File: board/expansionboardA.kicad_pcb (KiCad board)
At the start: 2 copper layers, 131 x 83.8 mm, 55 parts, among them J1 USB_C_Receptacle, J3 HDMI_A, SW4 ESPPROG, U1 ESP32-S3-WROOM-1, U2 GPIO_U2, U3 SII164CTG64, U4 GPIO_U4, U6 CS4344-CZZR

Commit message: Updates to board files
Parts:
- added REF**: Fiducial_0.5mm_Mask1.5mm, Fiducial:Fiducial_0.5mm_Mask1.5mm, B.Cu at (130.9, 78.7)
- added REF**: Fiducial_0.5mm_Mask1.5mm, Fiducial:Fiducial_0.5mm_Mask1.5mm, B.Cu at (74.5, 61.3)
- added REF**: Fiducial_0.5mm_Mask1.5mm, Fiducial:Fiducial_0.5mm_Mask1.5mm, B.Cu at (122.2, 59.7)
- added REF**: Fiducial_0.5mm_Mask1.5mm, Fiducial:Fiducial_0.5mm_Mask1.5mm, B.Cu at (132.6, 96.2)
- added REF**: Fiducial_0.5mm_Mask1.5mm, Fiducial:Fiducial_0.5mm_Mask1.5mm, B.Cu at (98.2, 74.2)
- added REF**: Fiducial_0.5mm_Mask1.5mm, Fiducial:Fiducial_0.5mm_Mask1.5mm, B.Cu at (32.0, 65.9)
- added t3V3: TestPoint, TestPoint:TestPoint_Pad_D1.0mm, B.Cu at (135.6, 53.2)
- added t5V0: TestPoint, TestPoint:TestPoint_Pad_D1.0mm, B.Cu at (112.6, 43.2)
- added tEN1: TestPoint, TestPoint:TestPoint_Pad_D1.0mm, B.Cu at (80.0, 52.5)
- added tPWR1: TestPoint, TestPoint:TestPoint_Pad_D1.0mm, B.Cu at (31.8, 91.1)
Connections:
- REF** pad 1: SHLD -> GND (x4)
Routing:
- net 5V: track 173.1 -> 180.1 mm
- net ESP_RST: track 42.2 -> 45.8 mm
- net REG3V3: track 228.3 -> 231.0 mm

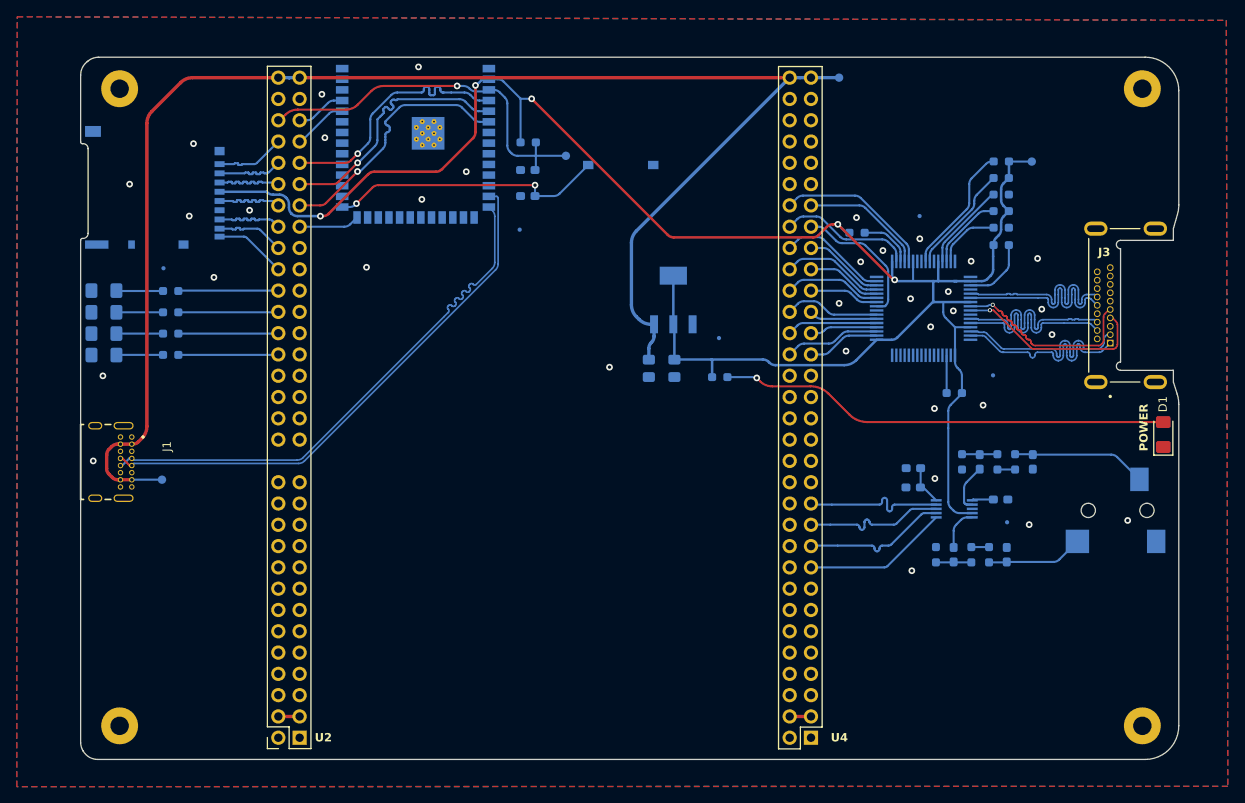
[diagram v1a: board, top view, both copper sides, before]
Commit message: Updated board and some typos in doc
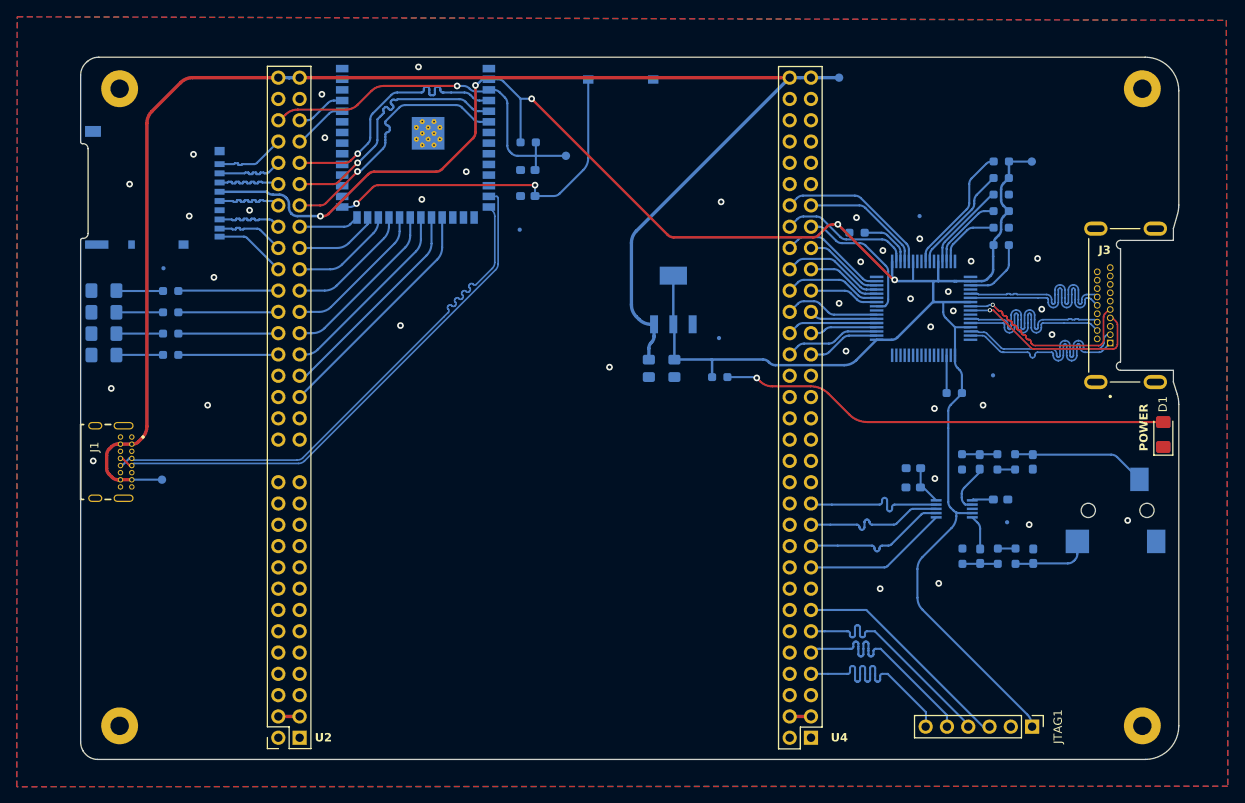
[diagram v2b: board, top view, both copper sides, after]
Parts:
- added JTAG1: Conn_01x06_Pin, Connector_PinHeader_2.54mm:PinHeader_1x06_P2.54mm_Vertical, F.Cu at (135.6, 120.6)
- moved REF** 52.1 mm to (78.0, 118.1)
- moved REF** 52.1 mm to (89.8, 118.4)
- moved REF** 52.1 mm to (83.9, 118.0)
- moved REF** 52.1 mm to (67.4, 118.0)
- moved SW4 10.2 mm to (86.5, 43.4)
- moved C13 3.17 mm to (129.4, 100.3)
- moved C9 3.17 mm to (135.7, 100.3)
- moved R12 3.17 mm to (131.5, 100.3)
- moved R8 3.17 mm to (133.6, 100.3)
- moved R11 3.17 mm to (127.3, 100.3)
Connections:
- U1 pad 18: unconnected-(U1-IO10-Pad18) -> IO10
- U1 pad 19: unconnected-(U1-IO11-Pad19) -> IO11
- U1 pad 20: unconnected-(U1-IO12-Pad20) -> IO12
- U1 pad 21: unconnected-(U1-IO13-Pad21) -> IO13
- U1 pad 22: unconnected-(U1-IO14-Pad22) -> IO14
- U1 pad 23: unconnected-(U1-IO21-Pad23) -> IO21
- U1 pad 24: unconnected-(U1-IO47-Pad24) -> IO47
- U1 pad 25: unconnected-(U1-IO48-Pad25) -> IO48
- U2 pad 33: unconnected-(U2-Pin_33-Pad33) -> IO10
- U2 pad 35: unconnected-(U2-Pin_35-Pad35) -> IO11
- U2 pad 37: unconnected-(U2-Pin_37-Pad37) -> IO12
- U2 pad 39: unconnected-(U2-Pin_39-Pad39) -> IO13
- U2 pad 41: unconnected-(U2-Pin_41-Pad41) -> IO14
- U2 pad 43: unconnected-(U2-Pin_43-Pad43) -> IO21
- U2 pad 45: unconnected-(U2-Pin_45-Pad45) -> IO47
- U2 pad 47: unconnected-(U2-Pin_47-Pad47) -> IO48
- U4 pad 11: unconnected-(U4-Pin_11-Pad11) -> TDO
- U4 pad 13: unconnected-(U4-Pin_13-Pad13) -> TCK
- U4 pad 7: unconnected-(U4-Pin_7-Pad7) -> TMS
- U4 pad 9: unconnected-(U4-Pin_9-Pad9) -> TDI
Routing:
- net REG3V3: track 231.0 -> 263.8 mm
- net IO10: track 0.00 -> 28.4 mm
- net TCK: track 0.00 -> 27.1 mm
- net TDO: track 0.00 -> 27.0 mm
- net TDI: track 0.00 -> 27.0 mm
- net TMS: track 0.00 -> 26.9 mm
- net IO11: track 0.00 -> 25.8 mm
- net IO12: track 0.00 -> 23.1 mm
- net IO13: track 0.00 -> 20.5 mm
- net IO14: track 0.00 -> 17.9 mm
- net IO21: track 0.00 -> 15.2 mm
- net IO47: track 0.00 -> 13.0 mm
- net Net-(U1-IO0): track 33.1 -> 43.2 mm
- net IO48: track 0.00 -> 10.00 mm
- net Net-(AU1-Pad2): track 11.5 -> 9.50 mm
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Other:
- board text added: "DVI 1.0"
- board text removed: "AA1"
- board text removed: "AA19"
- board text removed: "AA20"
- board text removed: "AA3"
- board text removed: "AB1"
- board text removed: "AB2"
- board text removed: "AB21"
- board text removed: "AB3"
- board text removed: "DVI 1.0 OUT"
- board text removed: "ESP32-S3-WROOM-1"
- board text removed: "H2"
- board text removed: "K1"
- board text removed: "K2"
- board text removed: "M1"
- board text removed: "N17"
- board text removed: "POWER & DATA"
- board text removed: "R18"
- board text removed: "R4"
- board text removed: "T1"
- board text removed: "T21"
- board text removed: "T4"
- board text removed: "T5"
- board text removed: "U1"
- board text removed: "U17"
- board text removed: "U20"
- board text removed: "U5"
- board text removed: "V18"
- board text removed: "V4"
- board text removed: "W1"
- board text removed: "W4"
- board text removed: "Y1"
- board text removed: "Y18"
- board text removed: "Y21"
- board text removed: "Y3"

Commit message: Board update
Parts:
- added REF**: Fiducial_0.5mm_Mask1.5mm, Fiducial:Fiducial_0.5mm_Mask1.5mm, B.Cu at (143.6, 44.2)
- added REF**: Fiducial_0.5mm_Mask1.5mm, Fiducial:Fiducial_0.5mm_Mask1.5mm, B.Cu at (143.4, 120.1)
- added REF**: Fiducial_0.5mm_Mask1.5mm, Fiducial:Fiducial_0.5mm_Mask1.5mm, B.Cu at (31.8, 44.2)
- added REF**: Fiducial_0.5mm_Mask1.5mm, Fiducial:Fiducial_0.5mm_Mask1.5mm, B.Cu at (31.8, 120.1)
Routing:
- net REG3V3: track 263.8 -> 264.7 mm
- net GND: vias 37 -> 42

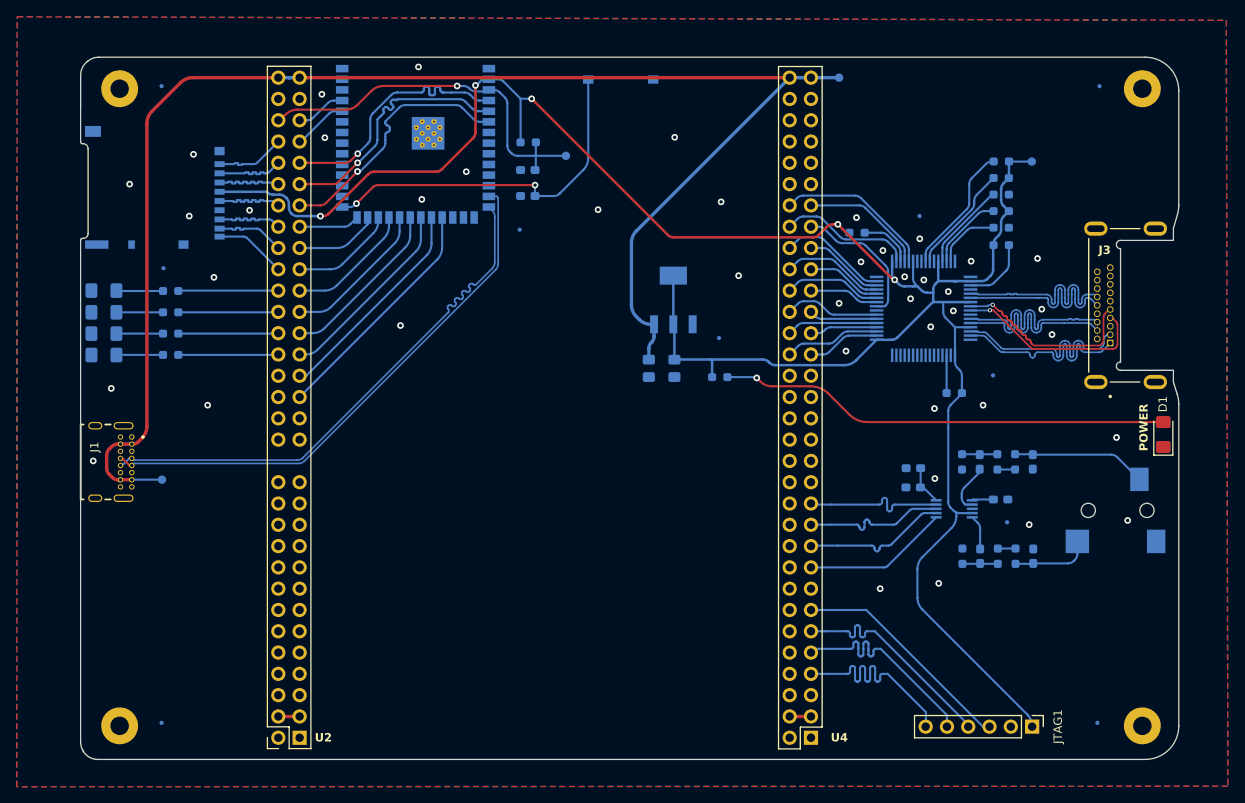
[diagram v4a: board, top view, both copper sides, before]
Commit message: Started to get rid of the video and audio chips and circuitry
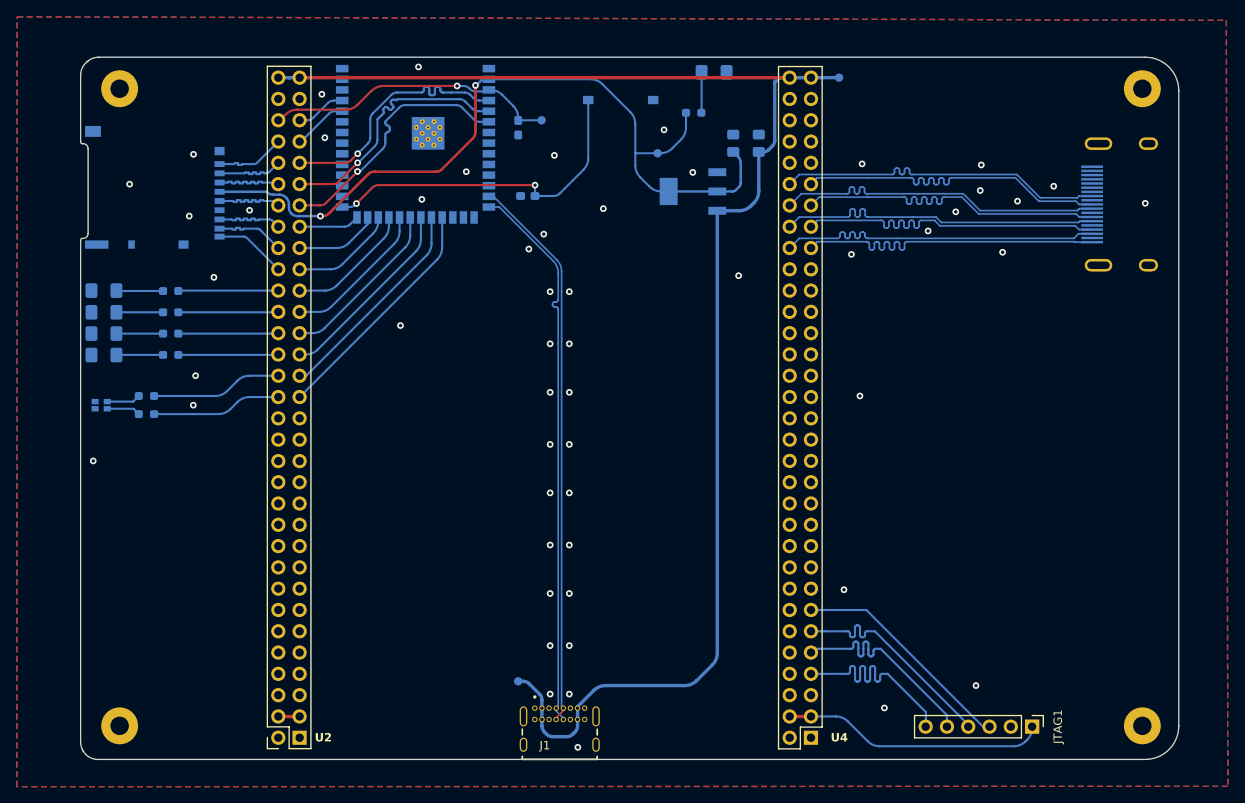
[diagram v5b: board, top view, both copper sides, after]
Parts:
- removed AU1: SJ-3523-SMT-TR, SJ-3523-SMT-TR:CUI_SJ-3523-SMT-TR
- removed C10: 0.1uf, Capacitor_SMD:C_0603_1608Metric_Pad1.08x0.95mm_HandSolder
- removed C11, C13, C14: 3.3uf, Capacitor_SMD:C_0603_1608Metric_Pad1.08x0.95mm_HandSolder
- removed C12: 10uf, Capacitor_SMD:C_0603_1608Metric_Pad1.08x0.95mm_HandSolder
- removed C8, C9: 1uf, Capacitor_SMD:C_0603_1608Metric_Pad1.08x0.95mm_HandSolder
- removed J3: HDMI_A, HD02-19-M-MSMT-TR:CUI_HD02-19-M-MSMT-TR
- removed R11, R14, R15, R18, R19, R20, R21, R22: 10KOhm, Resistor_SMD:R_0603_1608Metric_Pad0.98x0.95mm_HandSolder
- removed R12, R13: 470Ohm, Resistor_SMD:R_0603_1608Metric_Pad0.98x0.95mm_HandSolder
- removed R23: 33KOhm, Resistor_SMD:R_0603_1608Metric_Pad0.98x0.95mm_HandSolder
- removed R24: 510Ohm, Resistor_SMD:R_0603_1608Metric_Pad0.98x0.95mm_HandSolder
- removed R8: 33Ohm, Resistor_SMD:R_0603_1608Metric_Pad0.98x0.95mm_HandSolder
- removed the REF** at (98.2, 74.2)
- removed the REF** at (32.0, 65.9)
- removed the REF** at (130.9, 78.7)
- removed the REF** at (74.5, 61.3)
- removed the REF** at (143.6, 44.2)
- removed the REF** at (143.4, 120.1)
- removed the REF** at (122.2, 59.7)
- removed the REF** at (31.8, 44.2)
- removed the REF** at (31.8, 120.1)
- removed the REF** at (132.6, 96.2)
- removed U6: CS4344-CZZR, footprints:CIR_3TSSOP-10
- added J2: 2086581051, HDMI_2086:MOLEX_2086581051, B.Cu at (153.1, 58.3)
- D1: moved to B.Cu
- R2: value 10KOhm -> 33Ohm
- U3: value SII164CTG64 -> LTST-C195KGJRKT; footprint SI164CTG64:QFP50P1200X1200X120-64N -> LED_LTST_C195KGJRKT:LTST-BILED-15X16
- moved R7 103.8 mm to (29.9, 83.3), turned to 180 degrees
- moved U3 98.8 mm to (24.5, 82.3), turned to 90 degrees
- moved REF** 80.0 mm to (146.8, 108.5), turned to -90 degrees
- moved REF** 71.8 mm to (146.9, 97.9), turned to -90 degrees
- moved D1 68.8 mm to (97.7, 42.5), turned to 180 degrees
- moved REF** 68.1 mm to (146.8, 92.0), turned to -90 degrees
- moved REF** 65.9 mm to (147.2, 86.1), turned to -90 degrees
- moved J1 64.9 mm to (79.3, 122.8), turned to 0 degrees
- moved R2 54.7 mm to (29.9, 81.2)
- moved tPWR1 48.8 mm to (74.3, 115.2), turned to 0 degrees
- moved t3V3 44.6 mm to (90.9, 52.2)
- moved R1 31.7 mm to (95.2, 47.4)
- moved C7 29.9 mm to (103.0, 51.0), turned to 90 degrees
- moved C6 27.8 mm to (99.9, 51.0), turned to 90 degrees
- moved VR1 13.2 mm to (95.1, 56.8), turned to 180 degrees
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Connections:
- JTAG1 pad 1: REG3V3 -> VCC
- R2 pad 1: ESP_RST -> STAT_G1
- R2 pad 2: REG3V3 -> Net-(R2-Pad2)
- R7 pad 1: LEFTOUT -> STAT_R1
- R7 pad 2: Net-(AU1-Pad3) -> Net-(R7-Pad2)
- U2 pad 34: unconnected-(U2-Pin_34-Pad34) -> STAT_R1
- U2 pad 36: unconnected-(U2-Pin_36-Pad36) -> STAT_G1
- U4 pad 37: VDAT11 -> unconnected-(U4-Pin_37-Pad37)
- U4 pad 38: VDAT10 -> unconnected-(U4-Pin_38-Pad38)
- U4 pad 39: VDAT9 -> unconnected-(U4-Pin_39-Pad39)
- U4 pad 40: VDAT8 -> unconnected-(U4-Pin_40-Pad40)
- U4 pad 41: VDAT7 -> unconnected-(U4-Pin_41-Pad41)
- U4 pad 42: VDAT6 -> unconnected-(U4-Pin_42-Pad42)
- U4 pad 43: VDAT5 -> unconnected-(U4-Pin_43-Pad43)
- U4 pad 44: VDAT4 -> unconnected-(U4-Pin_44-Pad44)
- U4 pad 45: VDAT3 -> unconnected-(U4-Pin_45-Pad45)
- U4 pad 46: VDAT2 -> unconnected-(U4-Pin_46-Pad46)
- U4 pad 47: VDAT1 -> D2_P
- U4 pad 48: VDAT0 -> D2_N
- U4 pad 49: VCLK -> D1_P
- U4 pad 50: VDE -> D1_N
- U4 pad 51: VHSYNC -> D0_P
- U4 pad 52: VVSYNC -> D0_N
- U4 pad 53: unconnected-(U4-Pin_53-Pad53) -> CK_P
- U4 pad 54: unconnected-(U4-Pin_54-Pad54) -> CK_N
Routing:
- net REG3V3: track 264.7 -> 96.9 mm, vias 5 -> 2
- net Net-(D1-A): track 53.8 -> 4.84 mm, vias 1 -> 0
- net VCC: track 2.54 -> 31.5 mm
- net VVSYNC: track 18.9 -> 0.00 mm
- net AU_SDIN: track 17.4 -> 0.00 mm
- net AU_MCLK: track 17.4 -> 0.00 mm
- net AU_SCLK: track 17.3 -> 0.00 mm
- net AU_LRCLK: track 17.3 -> 0.00 mm
- net D0_N: track 23.1 -> 39.9 mm, vias 1 -> 0
- net VCLK: track 16.7 -> 0.00 mm
- net D0_P: track 23.4 -> 39.8 mm, vias 1 -> 0
- net VDE: track 16.0 -> 0.00 mm
- net Net-(AU1-Pad3): track 16.0 -> 0.00 mm
- net STAT_G1: track 0.00 -> 15.6 mm
- net STAT_R1: track 0.00 -> 15.5 mm
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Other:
- outline, holes or cut-outs redrawn
- board text added: "tinysys issue 2H December 2024 Engin Cilasun"
- board text removed: "tinysys issue 2G December 2024 Engin Cilasun"
